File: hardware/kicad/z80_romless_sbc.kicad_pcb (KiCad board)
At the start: 2 copper layers, 180 x 135 mm, 69 parts, among them J1 REGULATED 5V INPUT, Q1 2N3904 MCP RESET, U1 Z84C0020PEC, U10 SN74LVC245AN bus-to-Pico, U2 AS6C1008-55PCN, U3 ATF22V10B/C, U4 SN74AHCT244N, U7 SN74LVC244AN, U8 MCP23S17-E/SP, U9 SN74AHCT245N Pico-to-bus

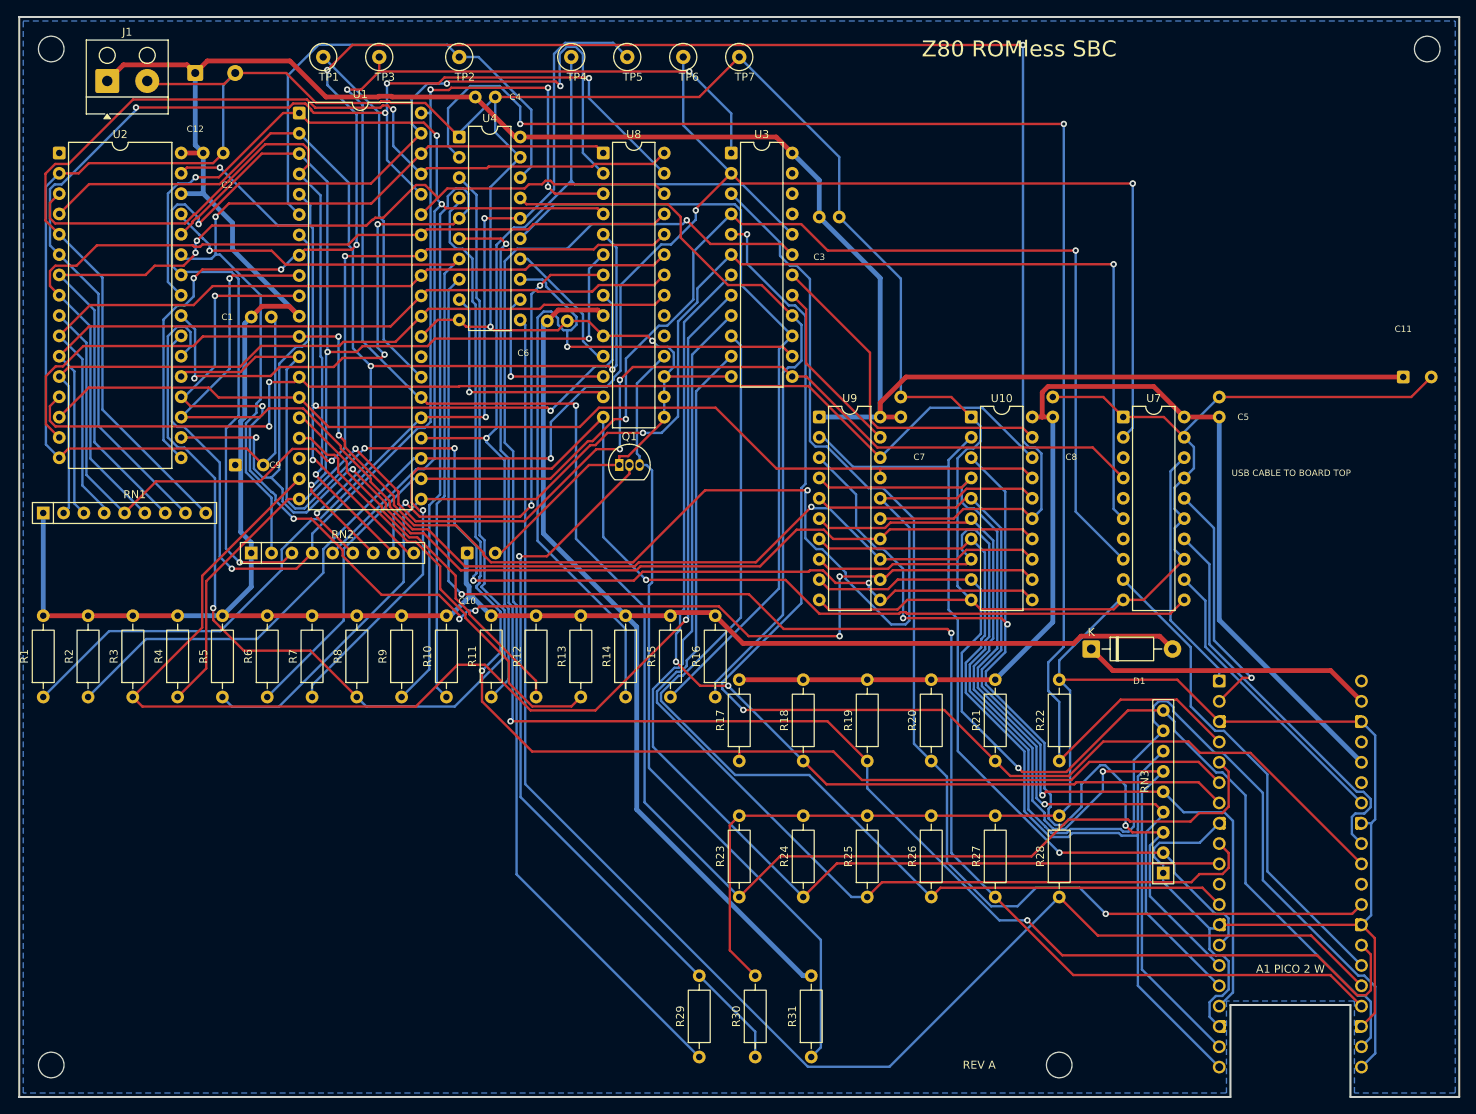
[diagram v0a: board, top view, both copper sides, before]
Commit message: Add Z80 ROMless SBC design documentation and update build scripts
- Created a new documentation file `medium.md` detailing the design process of the Z80 ROMless SBC using GitHub Copilot and KiCad.
- Updated `build-kicad-pcb.py` to refine component placements, adjust antenna cutout dimensions, and implement a clock preroute for the Z80.
- Modified `build-kicad.sh` to include a command for syncing project rules with the KiCad project.
- Enhanced the PCB design validation process by adding checks for USB connector alignment and antenna keepout areas.
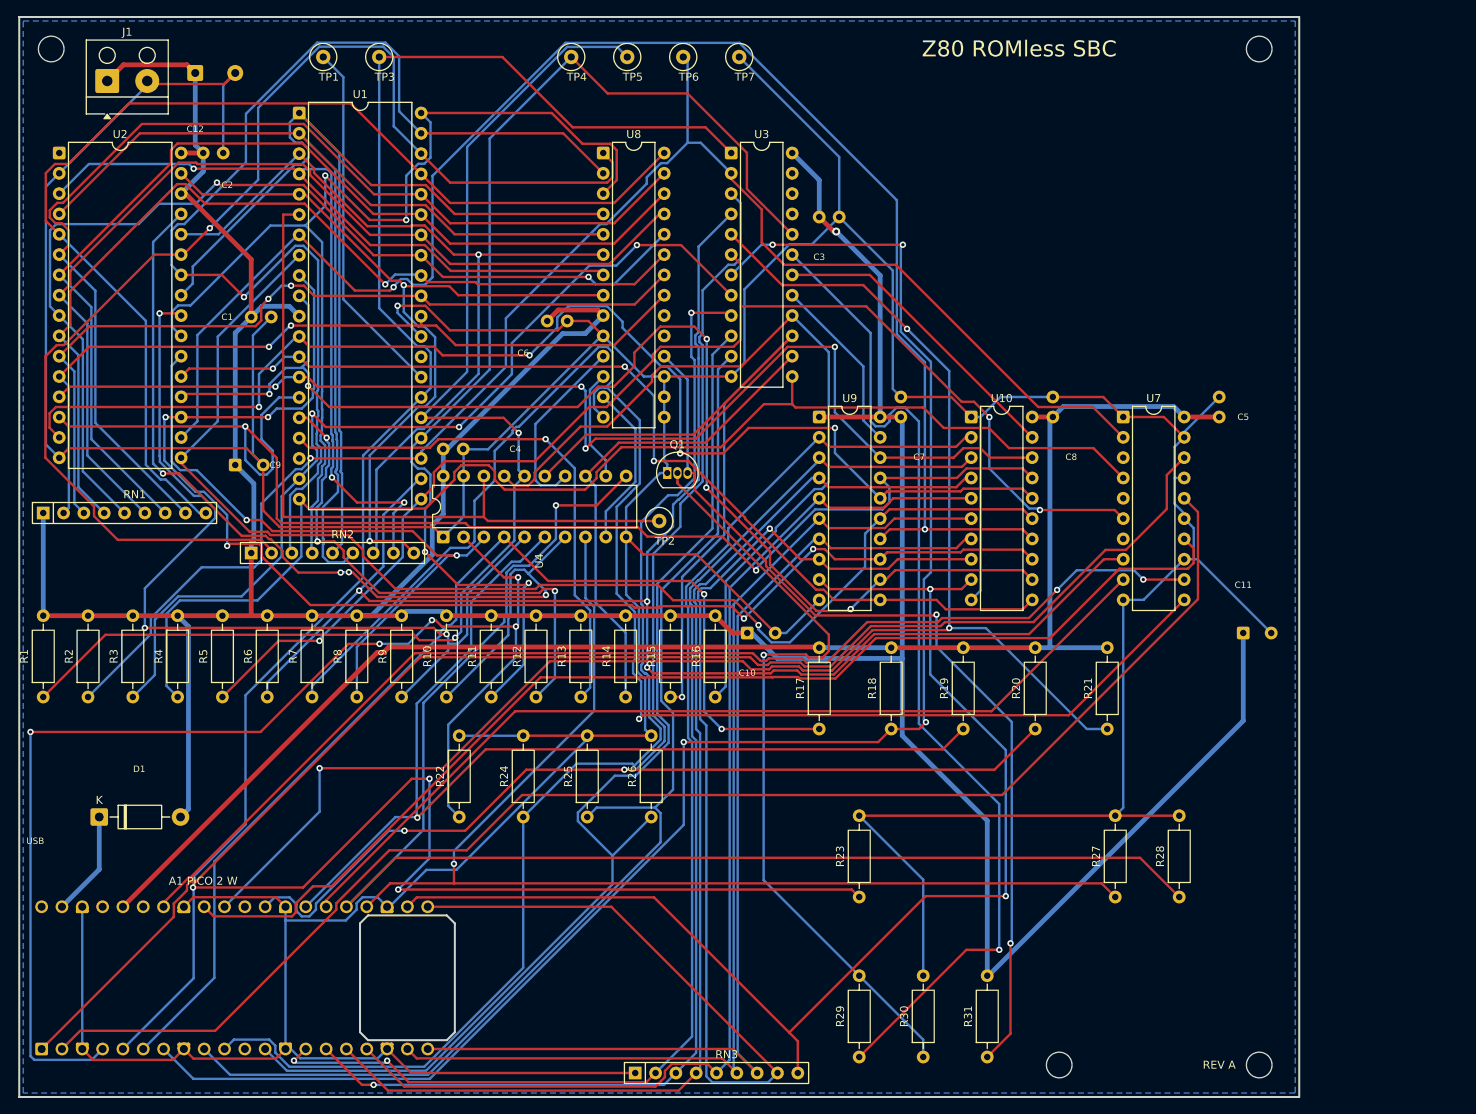
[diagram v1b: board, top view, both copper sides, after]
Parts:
- moved A1 154.2 mm to (7.80, 134.0), turned to 90 degrees
- moved H3 151.0 mm to (160.0, 136.0)
- moved D1 125.8 mm to (15.0, 105.0)
- moved R22 75.3 mm to (60.0, 105.0)
- moved RN3 70.6 mm to (82.0, 137.0), turned to 0 degrees
- moved TP2 63.2 mm to (85.0, 68.0)
- moved U4 50.0 mm to (58.0, 70.0), turned to 90 degrees
- moved C4 44.2 mm to (58.0, 59.0)
- moved C11 37.7 mm to (158.0, 82.0)
- moved C10 36.4 mm to (96.0, 82.0)
- moved R24 36.4 mm to (68.0, 105.0)
- moved R25 36.4 mm to (76.0, 105.0)
- moved R26 36.4 mm to (84.0, 105.0)
- moved R31 22.0 mm to (126.0, 135.0)
- moved H2 21.0 mm to (160.0, 9.00)
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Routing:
- net PICO_IORQ_N: track 31.2 -> 179.1 mm, vias 1 -> 0
- net PICO_BUSACK_N: track 31.2 -> 178.5 mm
- net PICO_WR_N: track 37.1 -> 147.0 mm, vias 0 -> 2
- net PICO_RD_N: track 50.4 -> 146.8 mm
- net D3: track 240.2 -> 158.8 mm, vias 5 -> 1
- net +5V: track 566.4 -> 485.9 mm, vias 0 -> 1
- net PICO_CE_N: track 126.7 -> 206.2 mm, vias 2 -> 4
- net SRAM_CE_N: track 151.7 -> 82.1 mm, vias 1 -> 2
- net PICO_SPI_CS_N: track 196.9 -> 133.7 mm, vias 3 -> 1
- net PICO_SPI_MISO: track 61.2 -> 117.1 mm
- net PICO_D0: track 105.6 -> 157.6 mm, vias 1 -> 2
- net A8: track 104.0 -> 154.9 mm
- net GND: track 750.7 -> 795.3 mm, vias 2 -> 1
- net PICO_SPI_SCK: track 190.5 -> 146.5 mm, vias 2 -> 1
- net D4: track 158.6 -> 200.8 mm
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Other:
- board size 180 x 135 mm -> 160 x 135 mm
- board text added: "USB"
- board text removed: "USB CABLE TO BOARD TOP"
